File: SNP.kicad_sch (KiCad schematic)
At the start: 9 parts, among them J1 SNP, U75 IN74ALS32N (КР1533ЛЛ1)

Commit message: March 22nd - 3rd edition
List 3 is complete
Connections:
- net GND: no longer J1.45
- net A12_SNP: no longer names the net of J1.44
- net A14_SNP: no longer names the net of J1.46
- net A15_SNP: no longer names the net of J1.47
- net A16_SNP: no longer names the net of J1.48
- net A28_SNP: no longer names the net of J1.60
- net A4_SNP: no longer names the net of J1.36
- net A7_SNP: no longer names the net of J1.39
- net B21_SNP: no longer names the net of J1.21
- net B22_SNP: no longer names the net of J1.22
- net B28_SNP: no longer names the net of J1.28
- net B29_SNP: no longer names the net of J1.29
- net B4_SNP: no longer names the net of J1.4
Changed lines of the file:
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@@
 (kicad_sch (version 20211123) (generator eeschema)
-  (paper "A3")
+  (paper "A4")
   (title_block
     (comment 2 "Евстафьев")
@@
     (stroke (width 0) (type default) (color 0 0 0 0))
   )
-  (wire (pts (xy 40.005 69.85) (xy 44.45 69.85))
-    (stroke (width 0) (type default) (color 0 0 0 0))
-  )
   (wire (pts (xy 173.99 46.355) (xy 173.99 50.165))
     (stroke (width 0) (type default) (color 0 0 0 0))
@@
     (stroke (width 0) (type default) (color 0 0 0 0))
   )
-  (wire (pts (xy 40.005 67.31) (xy 44.45 67.31))
-    (stroke (width 0) (type default) (color 0 0 0 0))
-  )
   (wire (pts (xy 138.43 46.355) (xy 138.43 70.485))
     (stroke (width 0) (type default) (color 0 0 0 0))
@@
     (stroke (width 0) (type default) (color 0 0 0 0))
   )
-  (wire (pts (xy 40.005 64.77) (xy 44.45 64.77))
-    (stroke (width 0) (type default) (color 0 0 0 0))
-  )
   (wire (pts (xy 128.27 46.355) (xy 128.27 60.325))
     (stroke (width 0) (type default) (color 0 0 0 0))
   )
-  (wire (pts (xy 69.215 85.09) (xy 62.23 85.09))
-    (stroke (width 0) (type default) (color 0 0 0 0))
-  )
   (wire (pts (xy 40.005 74.93) (xy 44.45 74.93))
     (stroke (width 0) (type default) (color 0 0 0 0))
@@
     (stroke (width 0) (type default) (color 0 0 0 0))
   )
-  (wire (pts (xy 69.215 102.87) (xy 62.23 102.87))
-    (stroke (width 0) (type default) (color 0 0 0 0))
-  )
   (wire (pts (xy 135.89 67.945) (xy 151.13 67.945))
     (stroke (width 0) (type default) (color 0 0 0 0))
@@
     (stroke (width 0) (type default) (color 0 0 0 0))
   )
-  (wire (pts (xy 40.005 62.23) (xy 44.45 62.23))
-    (stroke (width 0) (type default) (color 0 0 0 0))
-  )
   (wire (pts (xy 133.35 46.355) (xy 133.35 65.405))
     (stroke (width 0) (type default) (color 0 0 0 0))
@@
     (stroke (width 0) (type default) (color 0 0 0 0))
   )
-  (wire (pts (xy 40.005 49.53) (xy 44.45 49.53))
-    (stroke (width 0) (type default) (color 0 0 0 0))
-  )
   (wire (pts (xy 124.46 88.265) (xy 151.13 88.265))
     (stroke (width 0) (type default) (color 0 0 0 0))
@@
     (stroke (width 0) (type default) (color 0 0 0 0))
   )
-  (wire (pts (xy 69.215 105.41) (xy 62.23 105.41))
-    (stroke (width 0) (type default) (color 0 0 0 0))
-  )
   (wire (pts (xy 128.27 98.425) (xy 128.27 100.965))
     (stroke (width 0) (type default) (color 0 0 0 0))
@@
     (stroke (width 0) (type default) (color 0 0 0 0))
   )
-  (wire (pts (xy 40.005 72.39) (xy 44.45 72.39))
-    (stroke (width 0) (type default) (color 0 0 0 0))
-  )
   (wire (pts (xy 40.005 52.07) (xy 44.45 52.07))
     (stroke (width 0) (type default) (color 0 0 0 0))
   )
-  (wire (pts (xy 69.215 87.63) (xy 62.23 87.63))
-    (stroke (width 0) (type default) (color 0 0 0 0))
-  )
   (wire (pts (xy 124.46 78.105) (xy 146.05 78.105))
     (stroke (width 0) (type default) (color 0 0 0 0))
   )
-  (wire (pts (xy 69.215 41.91) (xy 62.23 41.91))
-    (stroke (width 0) (type default) (color 0 0 0 0))
-  )
   (wire (pts (xy 40.005 97.79) (xy 44.45 97.79))
     (stroke (width 0) (type default) (color 0 0 0 0))
@@
     (stroke (width 0) (type default) (color 0 0 0 0))
   )
-  (wire (pts (xy 40.005 102.87) (xy 44.45 102.87))
-    (stroke (width 0) (type default) (color 0 0 0 0))
-  )
   (wire (pts (xy 190.5 57.15) (xy 190.5 55.245))
     (stroke (width 0) (type default) (color 0 0 0 0))
@@
   )
   (wire (pts (xy 155.575 36.195) (xy 173.99 36.195))
-    (stroke (width 0) (type default) (color 0 0 0 0))
-  )
-  (wire (pts (xy 40.005 41.91) (xy 44.45 41.91))
     (stroke (width 0) (type default) (color 0 0 0 0))
   )
@@
     )
   )
-  (global_label "A7_SNP" (shape input) (at 40.005 49.53 180) (fields_autoplaced)
-    (effects (font (size 1.27 1.27)) (justify right))
-    (property "Intersheet References" "${INTERSHEET_REFS}" (id 0) (at 30.5162 49.4506 0)
-      (effects (font (size 1.27 1.27)) (justify right) hide)
-    )
-  )
-  (global_label "A16_SNP" (shape input) (at 40.005 72.39 180) (fields_autoplaced)
-    (effects (font (size 1.27 1.27)) (justify right))
-    (property "Intersheet References" "${INTERSHEET_REFS}" (id 0) (at 29.3067 72.3106 0)
-      (effects (font (size 1.27 1.27)) (justify right) hide)
-    )
-  )
   (global_label "A26_SNP" (shape input) (at 40.005 97.79 180) (fields_autoplaced)
     (effects (font (size 1.27 1.27)) (justify right))
@@
     )
   )
-  (global_label "B22_SNP" (shape input) (at 69.215 87.63 0) (fields_autoplaced)
-    (effects (font (size 1.27 1.27)) (justify left))
-    (property "Intersheet References" "${INTERSHEET_REFS}" (id 0) (at 80.0948 87.5506 0)
-      (effects (font (size 1.27 1.27)) (justify left) hide)
-    )
-  )
-  (global_label "B4_SNP" (shape input) (at 69.215 41.91 0) (fields_autoplaced)
-    (effects (font (size 1.27 1.27)) (justify left))
-    (property "Intersheet References" "${INTERSHEET_REFS}" (id 0) (at 78.8852 41.8306 0)
-      (effects (font (size 1.27 1.27)) (justify left) hide)
-    )
-  )
   (global_label "A18_SNP" (shape input) (at 40.005 77.47 180) (fields_autoplaced)
     (effects (font (size 1.27 1.27)) (justify right))
@@
     )
   )
-  (global_label "A12_SNP" (shape input) (at 40.005 62.23 180) (fields_autoplaced)
-    (effects (font (size 1.27 1.27)) (justify right))
-    (property "Intersheet References" "${INTERSHEET_REFS}" (id 0) (at 29.3067 62.1506 0)
-      (effects (font (size 1.27 1.27)) (justify right) hide)
-    )
-  )
   (global_label "ЗАПРШL" (shape input) (at 194.31 52.705 0) (fields_autoplaced)
     (effects (font (size 1.27 1.27)) (justify left))
@@
     )
   )
-  (global_label "A14_SNP" (shape input) (at 40.005 67.31 180) (fields_autoplaced)
-    (effects (font (size 1.27 1.27)) (justify right))
-    (property "Intersheet References" "${INTERSHEET_REFS}" (id 0) (at 29.3067 67.2306 0)
-      (effects (font (size 1.27 1.27)) (justify right) hide)
-    )
-  )
   (global_label "B9_SNP" (shape input) (at 69.215 54.61 0) (fields_autoplaced)
     (effects (font (size 1.27 1.27)) (justify left))
@@
     )
   )
-  (global_label "A28_SNP" (shape input) (at 40.005 102.87 180) (fields_autoplaced)
-    (effects (font (size 1.27 1.27)) (justify right))
-    (property "Intersheet References" "${INTERSHEET_REFS}" (id 0) (at 29.3067 102.7906 0)
-      (effects (font (size 1.27 1.27)) (justify right) hide)
-    )
-  )
   (global_label "A6_SNP" (shape input) (at 124.46 98.425 180) (fields_autoplaced)
     (effects (font (size 1.27 1.27)) (justify right))
@@
     )
   )
-  (global_label "B21_SNP" (shape input) (at 69.215 85.09 0) (fields_autoplaced)
-    (effects (font (size 1.27 1.27)) (justify left))
-    (property "Intersheet References" "${INTERSHEET_REFS}" (id 0) (at 80.0948 85.0106 0)
-      (effects (font (size 1.27 1.27)) (justify left) hide)
-    )
-  )
   (global_label "B9_SNP" (shape input) (at 124.46 73.025 180) (fields_autoplaced)
     (effects (font (size 1.27 1.27)) (justify right))
@@
     )
   )
-  (global_label "B29_SNP" (shape input) (at 69.215 105.41 0) (fields_autoplaced)
-    (effects (font (size 1.27 1.27)) (justify left))
-    (property "Intersheet References" "${INTERSHEET_REFS}" (id 0) (at 80.0948 105.3306 0)
-      (effects (font (size 1.27 1.27)) (justify left) hide)
-    )
-  )
   (global_label "B8_SNP" (shape input) (at 69.215 52.07 0) (fields_autoplaced)
     (effects (font (size 1.27 1.27)) (justify left))
@@
     )
   )
-  (global_label "B28_SNP" (shape input) (at 69.215 102.87 0) (fields_autoplaced)
-    (effects (font (size 1.27 1.27)) (justify left))
-    (property "Intersheet References" "${INTERSHEET_REFS}" (id 0) (at 80.0948 102.7906 0)
-      (effects (font (size 1.27 1.27)) (justify left) hide)
-    )
-  )
   (global_label "A29_SNP" (shape input) (at 40.005 105.41 180) (fields_autoplaced)
     (effects (font (size 1.27 1.27)) (justify right))
@@
     )
   )
-  (global_label "A15_SNP" (shape input) (at 40.005 69.85 180) (fields_autoplaced)
-    (effects (font (size 1.27 1.27)) (justify right))
-    (property "Intersheet References" "${INTERSHEET_REFS}" (id 0) (at 29.3067 69.7706 0)
-      (effects (font (size 1.27 1.27)) (justify right) hide)
-    )
-  )
   (global_label "A23_SNP" (shape input) (at 40.005 90.17 180) (fields_autoplaced)
     (effects (font (size 1.27 1.27)) (justify right))
@@
     )
   )
-  (global_label "A4_SNP" (shape input) (at 40.005 41.91 180) (fields_autoplaced)
-    (effects (font (size 1.27 1.27)) (justify right))
-    (property "Intersheet References" "${INTERSHEET_REFS}" (id 0) (at 30.5162 41.8306 0)
-      (effects (font (size 1.27 1.27)) (justify right) hide)
-    )
-  )
   (global_label "A30_SNP" (shape input) (at 40.005 107.95 180) (fields_autoplaced)
     (effects (font (size 1.27 1.27)) (justify right))
@@
     )
   )
-  (global_label "A13_SNP" (shape input) (at 40.005 64.77 180) (fields_autoplaced)
-    (effects (font (size 1.27 1.27)) (justify right))
-    (property "Intersheet References" "${INTERSHEET_REFS}" (id 0) (at 29.3067 64.6906 0)
-      (effects (font (size 1.27 1.27)) (justify right) hide)
-    )
-  )

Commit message: March 23rd Update 1
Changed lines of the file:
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@@
   )
   (symbol (lib_id "74xx:74LS32") (at 149.86 134.62 0) (unit 3)
-    (in_bom yes) (on_board yes) (fields_autoplaced)
-    (property "Reference" "U75" (id 0) (at 149.86 125.095 0))
+    (in_bom yes) (on_board yes)
+    (property "Reference" "U75" (id 0) (at 150.495 134.62 0))
     (property "Value" "IN74ALS32N (КР1533ЛЛ1)" (id 1) (at 149.86 127.635 0))
     (property "Footprint" "Package_DIP:DIP-14_W7.62mm_Socket_LongPads" (id 2) (at 149.86 134.62 0)
@@
   )
   (symbol (lib_id "74xx:74LS32") (at 130.175 132.08 0) (unit 2)
-    (in_bom yes) (on_board yes) (fields_autoplaced)
-    (property "Reference" "U75" (id 0) (at 130.175 123.19 0))
+    (in_bom yes) (on_board yes)
+    (property "Reference" "U75" (id 0) (at 130.175 132.08 0))
     (property "Value" "IN74ALS32N (КР1533ЛЛ1)" (id 1) (at 130.175 125.73 0))
     (property "Footprint" "Package_DIP:DIP-14_W7.62mm_Socket_LongPads" (id 2) (at 130.175 132.08 0)

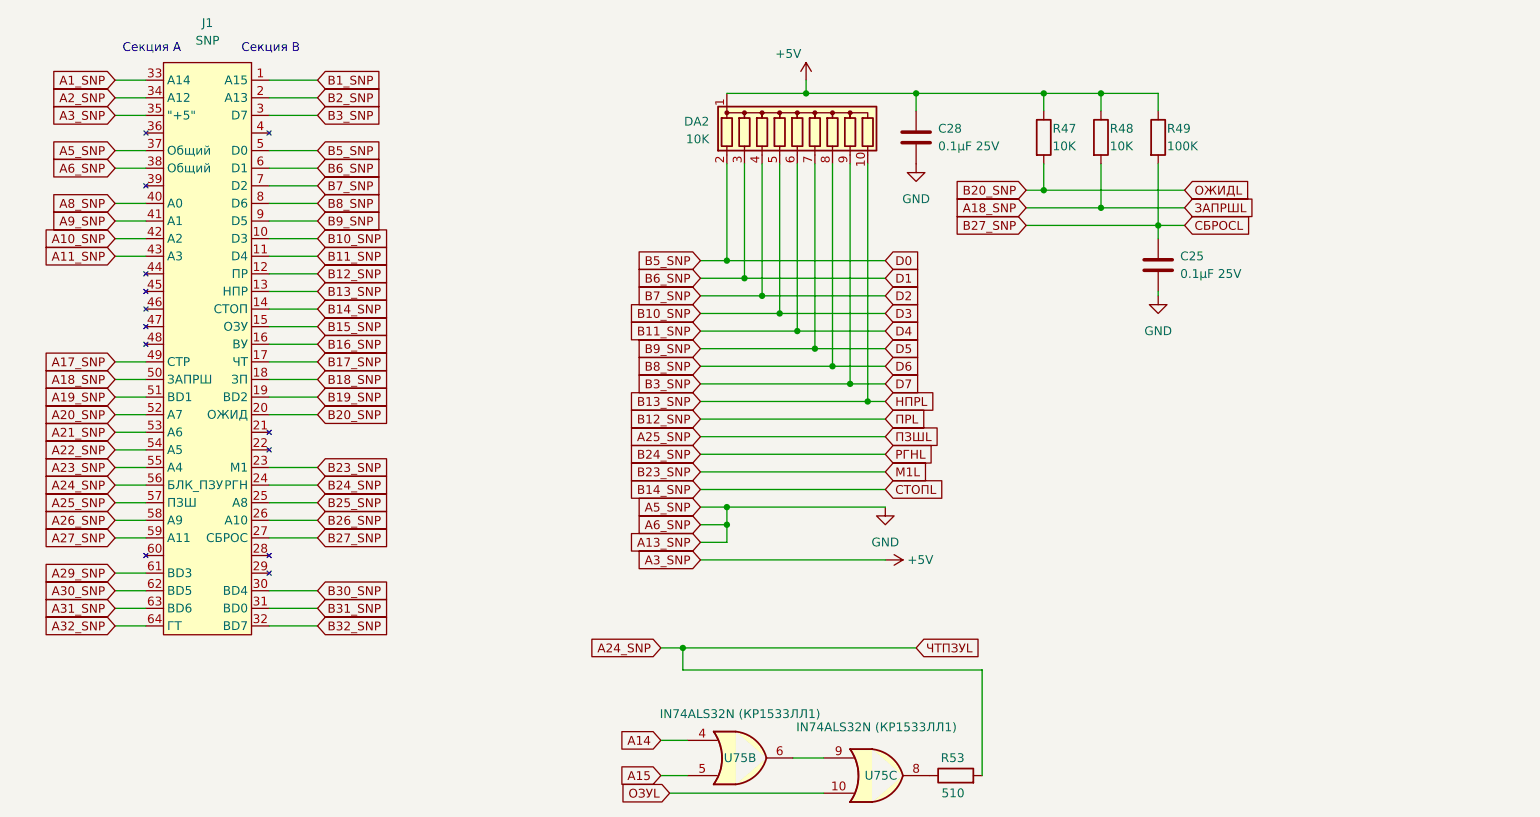
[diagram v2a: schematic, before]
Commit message: March 23rd First pre-alpha
First time ZERO errors and 93 warnings. Schematics are done, now to deal with warnings and footprints.
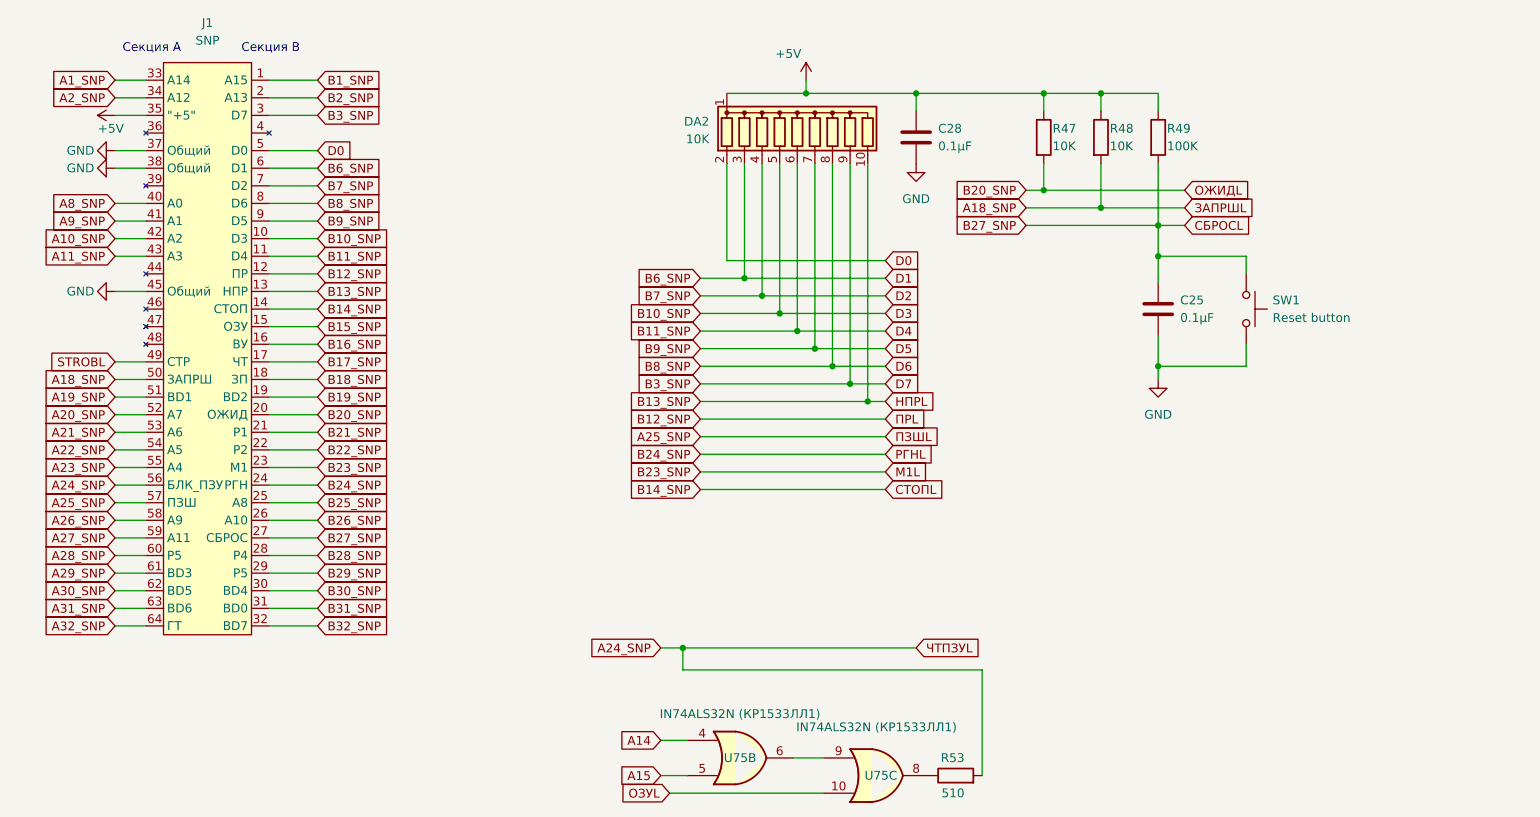
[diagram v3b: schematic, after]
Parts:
- added SW1: Reset button, Button_Switch_THT:SW_Tactile_SPST_Angled_PTS645Vx83-2LFS, symbol Switch:SW_Push
- C25, C28: value 0.1μF 25V -> 0.1μF; footprint (none) -> Capacitor_THT:C_Disc_D7.0mm_W2.5mm_P5.00mm
- R47, R48, R49, R53: footprint (none) -> Resistor_THT:R_Axial_DIN0207_L6.3mm_D2.5mm_P10.16mm_Horizontal
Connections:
- net B27_SNP: now also SW1.1
- net GND: now also J1.45 (Общий), SW1.2
- net B21_SNP: now reaches J1.21 (P1)
- net B22_SNP: now reaches J1.22 (P2)
- net B28_SNP: now reaches J1.28 (P4)
- net B29_SNP: now reaches J1.29 (P5)
- net A28_SNP: now reaches J1.60 (P5)
- net A17_SNP renamed STROBL
- net B5_SNP renamed D0
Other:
- moved on the sheet: C25

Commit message: March 24th - First Edition of PCB
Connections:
- net A1_SNP is gone; now on net A14: J1.33 (A14)
- net B15_SNP is gone; now on net ОЗУL: J1.15 (ОЗУ)
- net B1_SNP is gone; now on net A15: J1.1 (A15)
- net A10_SNP renamed A2
- net A11_SNP renamed A3
- net A18_SNP renamed ЗАПРШL
- net A20_SNP renamed A7
- net A21_SNP renamed A6
- net A22_SNP renamed A5
- net A23_SNP renamed A4
- net A24_SNP renamed ЧТПЗУL
- net A25_SNP renamed ПЗШL
- net A26_SNP renamed A9
- net A27_SNP renamed A11
- net A2_SNP renamed A12
- net A32_SNP renamed BUSY
- net A8_SNP renamed A0
- net A9_SNP renamed A1
- net B10_SNP renamed D3
- net B11_SNP renamed D4
- net B12_SNP renamed ПРL
- net B13_SNP renamed НПРL
- net B14_SNP renamed СТОПL
- net B16_SNP renamed ВУL
- net B17_SNP renamed ЧТL
- net B18_SNP renamed ЗПL
- net B20_SNP renamed ОЖИДL
- net B23_SNP renamed M1L
- net B24_SNP renamed РГНL
- net B25_SNP renamed A8
- net B26_SNP renamed A10
- net B27_SNP renamed СБРОСL
- net B2_SNP renamed A13
- net B3_SNP renamed D7
- net B6_SNP renamed D1
- net B7_SNP renamed D2
- net B8_SNP renamed D6
- net B9_SNP renamed D5

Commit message: March 24th Second Update
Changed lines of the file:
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@@
-    (stroke (width 0) (type default) (color 0 0 0 0))
-  )
-  (wire (pts (xy 121.92 116.205) (xy 121.92 119.38))
     (stroke (width 0) (type default) (color 0 0 0 0))
   )
@@
     (stroke (width 0) (type default) (color 0 0 0 0))
   )
-  (wire (pts (xy 165.1 119.38) (xy 121.92 119.38))
-    (stroke (width 0) (type default) (color 0 0 0 0))
-  )
   (wire (pts (xy 40.005 80.01) (xy 44.45 80.01))
     (stroke (width 0) (type default) (color 0 0 0 0))
@@
     (stroke (width 0) (type default) (color 0 0 0 0))
   )
+  (wire (pts (xy 168.275 134.62) (xy 165.1 134.62))
+    (stroke (width 0) (type default) (color 0 0 0 0))
+  )
   (wire (pts (xy 40.005 97.79) (xy 44.45 97.79))
     (stroke (width 0) (type default) (color 0 0 0 0))
@@
     (stroke (width 0) (type default) (color 0 0 0 0))
   )
-  (wire (pts (xy 121.92 116.205) (xy 155.575 116.205))
-    (stroke (width 0) (type default) (color 0 0 0 0))
-  )
   (wire (pts (xy 69.215 107.95) (xy 62.23 107.95))
     (stroke (width 0) (type default) (color 0 0 0 0))
@@
   )
   (wire (pts (xy 69.215 62.23) (xy 62.23 62.23))
-    (stroke (width 0) (type default) (color 0 0 0 0))
-  )
-  (wire (pts (xy 165.1 134.62) (xy 165.1 119.38))
     (stroke (width 0) (type default) (color 0 0 0 0))
   )
@@
     )
   )
+  (global_label "ЧТПЗУL" (shape input) (at 168.275 134.62 0) (fields_autoplaced)
+    (effects (font (size 1.27 1.27)) (justify left))
+    (property "Intersheet References" "${INTERSHEET_REFS}" (id 0) (at 177.6429 134.6994 0)
+      (effects (font (size 1.27 1.27)) (justify left) hide)
+    )
+  )
   (global_label "НПРL" (shape input) (at 151.13 80.645 0) (fields_autoplaced)
     (effects (font (size 1.27 1.27)) (justify left))
@@
     (property "Intersheet References" "${INTERSHEET_REFS}" (id 0) (at 29.3067 105.3306 0)
       (effects (font (size 1.27 1.27)) (justify right) hide)
-    )
-  )
-  (global_label "ЧТПЗУL" (shape input) (at 155.575 116.205 0) (fields_autoplaced)
-    (effects (font (size 1.27 1.27)) (justify left))
-    (property "Intersheet References" "${INTERSHEET_REFS}" (id 0) (at 164.9429 116.2844 0)
-      (effects (font (size 1.27 1.27)) (justify left) hide)
     )
   )
@@
       (effects (font (size 1.27 1.27)) (justify left))
     )
-    (property "Value" "510" (id 1) (at 162.56 137.16 90)
+    (property "Value" "510" (id 1) (at 163.195 134.62 90)
       (effects (font (size 1.27 1.27)) (justify left))
     )

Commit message: March 26th update
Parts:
- J1: footprint zxspectrum:SNP96 -> w_conn_av:snp59_96_female_angle_2
- U75: footprint Package_DIP:DIP-14_W7.62mm_Socket_LongPads -> Package_DIP:DIP-14_W7.62mm_Socket
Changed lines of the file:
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@@
     (property "Reference" "U75" (id 0) (at 150.495 134.62 0))
     (property "Value" "IN74ALS32N (КР1533ЛЛ1)" (id 1) (at 149.86 127.635 0))
-    (property "Footprint" "Package_DIP:DIP-14_W7.62mm_Socket_LongPads" (id 2) (at 149.86 134.62 0)
+    (property "Footprint" "Package_DIP:DIP-14_W7.62mm_Socket" (id 2) (at 149.86 134.62 0)
       (effects (font (size 1.27 1.27)) hide)
     )
@@
     (property "Reference" "J1" (id 0) (at 53.34 26.035 0))
     (property "Value" "SNP" (id 1) (at 53.34 28.575 0))
-    (property "Footprint" "zxspectrum:SNP96" (id 2) (at 53.34 27.94 0)
+    (property "Footprint" "w_conn_av:snp59_96_female_angle_2" (id 2) (at 53.34 27.94 0)
       (effects (font (size 1.27 1.27)) hide)
     )
@@
     (property "Reference" "U75" (id 0) (at 130.175 132.08 0))
     (property "Value" "IN74ALS32N (КР1533ЛЛ1)" (id 1) (at 130.175 125.73 0))
-    (property "Footprint" "Package_DIP:DIP-14_W7.62mm_Socket_LongPads" (id 2) (at 130.175 132.08 0)
+    (property "Footprint" "Package_DIP:DIP-14_W7.62mm_Socket" (id 2) (at 130.175 132.08 0)
       (effects (font (size 1.27 1.27)) hide)
     )

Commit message: 28th march ver2
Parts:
- added C26, C27: 0.1μF, Capacitor_THT:C_Disc_D7.0mm_W2.5mm_P5.00mm, symbol Device:C
- J1: footprint w_conn_av:snp59_96_female_angle_2 -> delta:snp59_96_female_angle_3
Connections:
- net +5V: now also C26.1, C27.1
- net GND: now also C26.2, C27.2
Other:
- moved on the sheet: C25, R47, R48, R49, SW1
